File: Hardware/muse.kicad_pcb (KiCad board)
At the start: 2 copper layers, 47 parts, among them P1 3.5mm_line, P2 3.5mm_line, P3 RCA, P4 RCA, P5 ATX_PWR_OK, P6 ATX_PWR_OK, P7 ATX_PWR_OK, P8 ATX_PS_ON, P9 LED_Signal, Q1 FQP30N06L, Q2 FQP30N06L, Q3 FQP30N06L, Q4 FQP30N06L, Q5 FQP30N06L, Q6 FQP30N06L, SW1 PWR_SW, U1 MSGEQ7, U2 MSGEQ7, U3 74LS595, U4 Spark_Core

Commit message: Preliminary PCB Layout in progress
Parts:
- D2: footprint LEDs:LED-5MM -> LEDs:LED-3MM
- P6: value ATX_PWR_OK -> ATX_PWR
- P7: value ATX_PWR_OK -> ATX_GND
- moved R2 103.7 mm to (43.8, 89.5), turned to 90 degrees
- moved U3 101.8 mm to (73.7, 39.4)
- moved P6 94.1 mm to (63.5, 86.4)
- moved D4 89.7 mm to (8.89, 64.8)
- moved D6 89.7 mm to (26.7, 64.8)
- moved D8 89.7 mm to (53.3, 66.0)
- moved P7 89.6 mm to (68.6, 86.4)
- moved P2 86.0 mm to (29.8, 91.1), turned to 90 degrees
- moved P4 85.7 mm to (26.1, 130.3), turned to 90 degrees
- moved P1 76.4 mm to (29.8, 85.7), turned to 90 degrees
- moved Q5 76.0 mm to (114.6, 101.6), turned to 90 degrees
- moved P5 73.8 mm to (73.7, 86.4)
- moved P3 70.7 mm to (26.1, 112.0), turned to 90 degrees
- moved P8 69.5 mm to (78.7, 86.4)
- moved C8 62.7 mm to (41.9, 118.1), turned to 90 degrees
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
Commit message: Preliminary board layout  complete
TODO: Route circuitry
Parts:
- D1, R1, R2, U3: moved to B.Cu
- Q1, Q2, Q3, Q4, Q5, Q6: footprint Transistors_TO-220:TO-220_Neutral123_Horizontal_LargePads -> Transistors_TO-220:TO-220_Neutral123_Vertical_LargePads
- moved D4 170.1 mm to (178.1, 81.8)
- moved D1 162.4 mm to (210.2, 62.9)
- moved P6 158.1 mm to (220.3, 66.7), turned to 270 degrees
- moved D6 156.2 mm to (181.9, 81.8)
- moved R1 153.3 mm to (186.1, 43.2), turned to 90 degrees
- moved P7 152.5 mm to (220.3, 71.1), turned to 270 degrees
- moved P8 149.8 mm to (220.3, 37.5)
- moved P9 147.5 mm to (220.3, 58.9)
- moved P5 147.1 mm to (220.3, 75.6), turned to 270 degrees
- moved R2 145.1 mm to (186.1, 61.0)
- moved SW1 144.9 mm to (220.3, 31.1), turned to 0 degrees
- moved U4 144.0 mm to (193.5, 31.0)
- moved C1 142.6 mm to (183.5, 43.2)
- moved C3 142.6 mm to (183.6, 35.6)
- moved C5 142.6 mm to (183.5, 40.6)
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
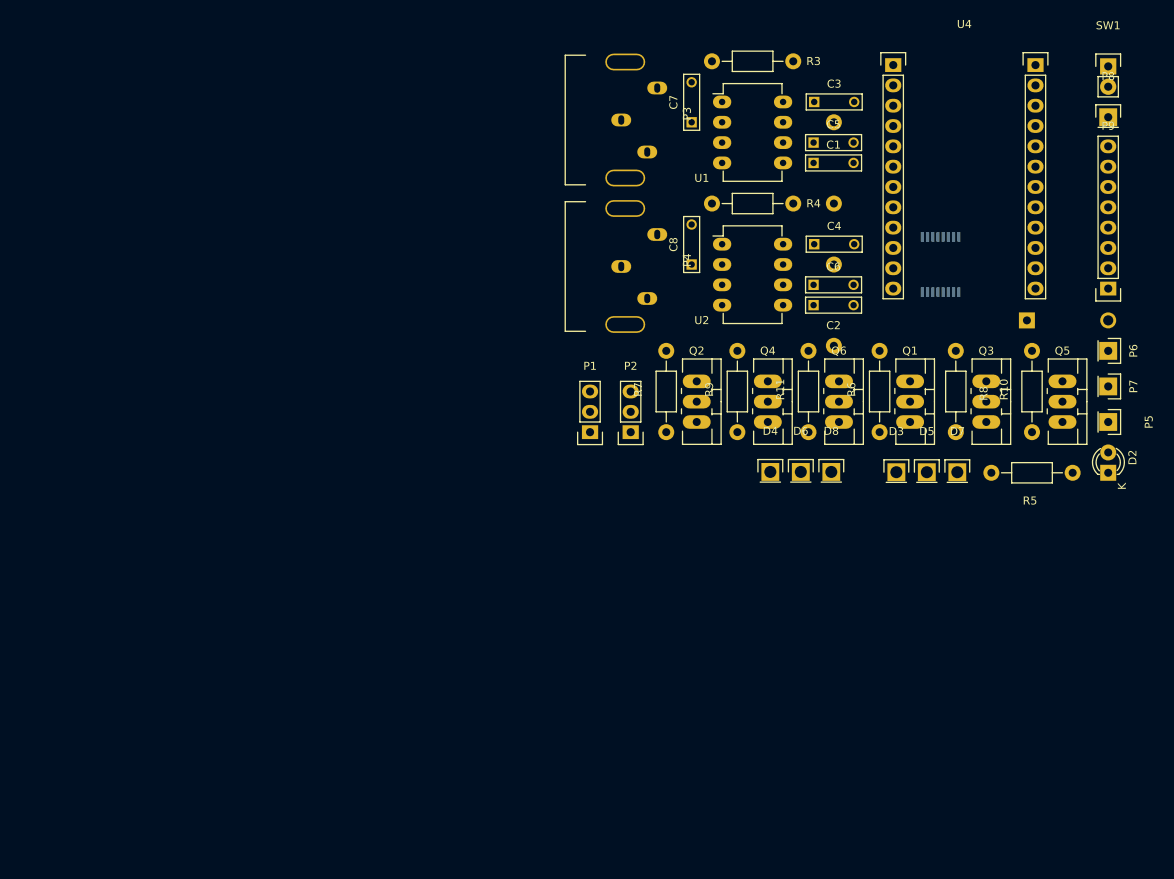
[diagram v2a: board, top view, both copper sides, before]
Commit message: Preliminary circuit made (sans gnd plane)
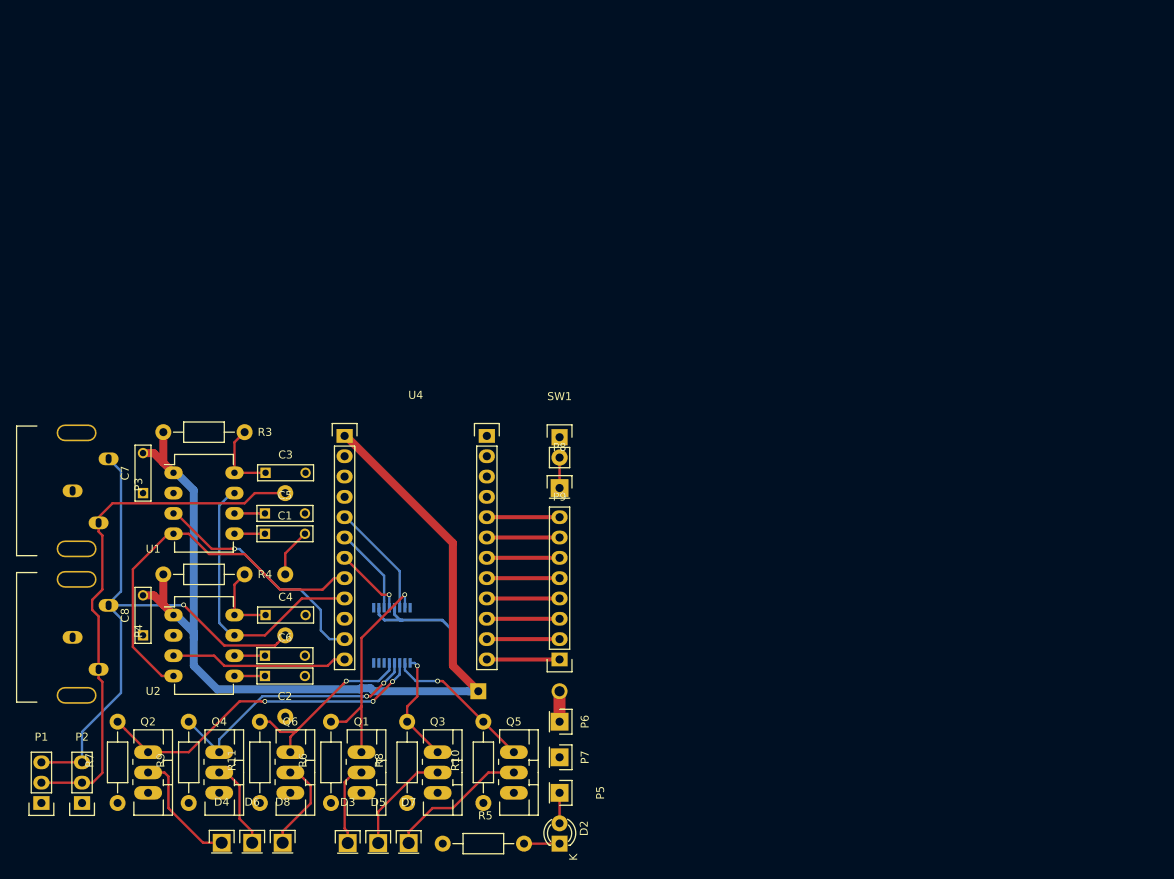
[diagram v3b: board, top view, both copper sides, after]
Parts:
- moved C7 82.8 mm to (99.7, 84.5)
- moved C8 82.8 mm to (99.7, 102.2)
- moved D1 82.8 mm to (141.6, 109.2)
- moved D2 82.8 mm to (151.8, 128.3)
- moved D3 82.8 mm to (125.3, 128.2)
- moved D5 82.8 mm to (129.1, 128.2)
- moved D7 82.8 mm to (132.9, 128.2)
- moved P5 82.8 mm to (151.8, 121.9)
- moved P6 82.8 mm to (151.8, 113.0)
- moved P7 82.8 mm to (151.8, 117.5)
- moved P8 82.8 mm to (151.8, 83.8)
- moved P9 82.8 mm to (151.8, 105.2)
- moved Q1 82.8 mm to (127.0, 119.4)
- moved Q4 82.8 mm to (109.2, 119.4)
- moved R1 82.8 mm to (117.5, 89.5)
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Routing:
- net +5V: track 0.00 -> 146.6 mm
- net /audio_r: track 0.00 -> 71.7 mm, vias 0 -> 1
- net /audio_l: track 0.00 -> 65.9 mm
- net /STROBE: track 0.00 -> 48.1 mm
- net /LED_1_R: track 0.00 -> 42.3 mm, vias 0 -> 3
- net /RST: track 0.00 -> 35.4 mm
- net /LED_1_G: track 0.00 -> 33.5 mm, vias 0 -> 2
- net /Aout_L: track 0.00 -> 29.4 mm, vias 0 -> 1
- net /LED_0_R: track 0.00 -> 28.2 mm, vias 0 -> 1
- net /LED_1_B: track 0.00 -> 24.2 mm, vias 0 -> 1
- net /Aout_R: track 0.00 -> 22.2 mm
- net /LED_0_B: track 0.00 -> 18.8 mm, vias 0 -> 1
- net Net-(D7-Pad1): track 0.00 -> 17.6 mm
- net Net-(D4-Pad1): track 0.00 -> 15.2 mm
- net /RGB_DAT: track 0.00 -> 14.3 mm
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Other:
- net class Default: trace_width 0.25 -> 0.3
- net class Power added: clearance 0.2, trace_width 1, via_dia 0.6, via_drill 0.4

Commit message: Completed muse v1.0 board
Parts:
- added ?: 1pin, Connect:1pin, F.Cu at (88.9, 128.3)
- added REF**: 1pin, Connect:1pin, F.Cu at (150.5, 128.3)
- added REF**: 1pin, Connect:1pin, F.Cu at (97.8, 74.9)
- added REF**: 1pin, Connect:1pin, F.Cu at (147.3, 74.9)
- moved PWR 8.89 mm to (142.9, 128.3), turned to 0 degrees
- moved B 7.62 mm to (125.3, 128.2)
- moved B 7.62 mm to (109.5, 128.2)
- moved G 7.62 mm to (105.7, 128.2)
- moved R 7.62 mm to (101.9, 128.2)
- moved R5 7.62 mm to (134.6, 128.3)
- moved G 7.62 mm to (121.5, 128.2)
- moved R 7.62 mm to (117.7, 128.2)
- renumbered P6 to +5V, D7 to B, D8 to B, D5 to G, D6 to G, P7 to GND, D2 to PWR, P5 to PWR_OK, D4 to R, D3 to R
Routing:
- net Net-(D7-Pad1): track 17.6 -> 24.4 mm
- net Net-(D2-Pad2): track 3.81 -> 10.5 mm
- net Net-(D5-Pad1): track 13.4 -> 18.7 mm
- net Net-(D3-Pad1): track 10.4 -> 14.2 mm
- net Net-(D4-Pad1): track 15.2 -> 11.4 mm
- net (no net): track 0.00 -> 2.54 mm, vias 0 -> 2
- net Net-(D8-Pad1): track 11.8 -> 13.8 mm
- net Net-(D2-Pad1): track 4.44 -> 3.18 mm
- net /Aout_L: track 29.4 -> 29.1 mm, vias 1 -> 2
- added copper zone on B.Cu, net GND
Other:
- board outline added: 71.6 x 61.5 mm
- board text added: "(1.0)"
- board text added: "Jason Merlo"
- board text added: "project muse"
